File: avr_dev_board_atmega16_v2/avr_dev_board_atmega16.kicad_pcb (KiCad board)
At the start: 2 copper layers, 100 x 79 mm, 28 parts, among them J1 AVR-ISP-10, J2 DC 7-15V, J3 PA(0-7), J4 PC(0-7), J5 PB(0-4), J6 +5V, J7 PD(0-7), SW1 RESET, U1 ATmega16A-PU, U2 LM1117-5.0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

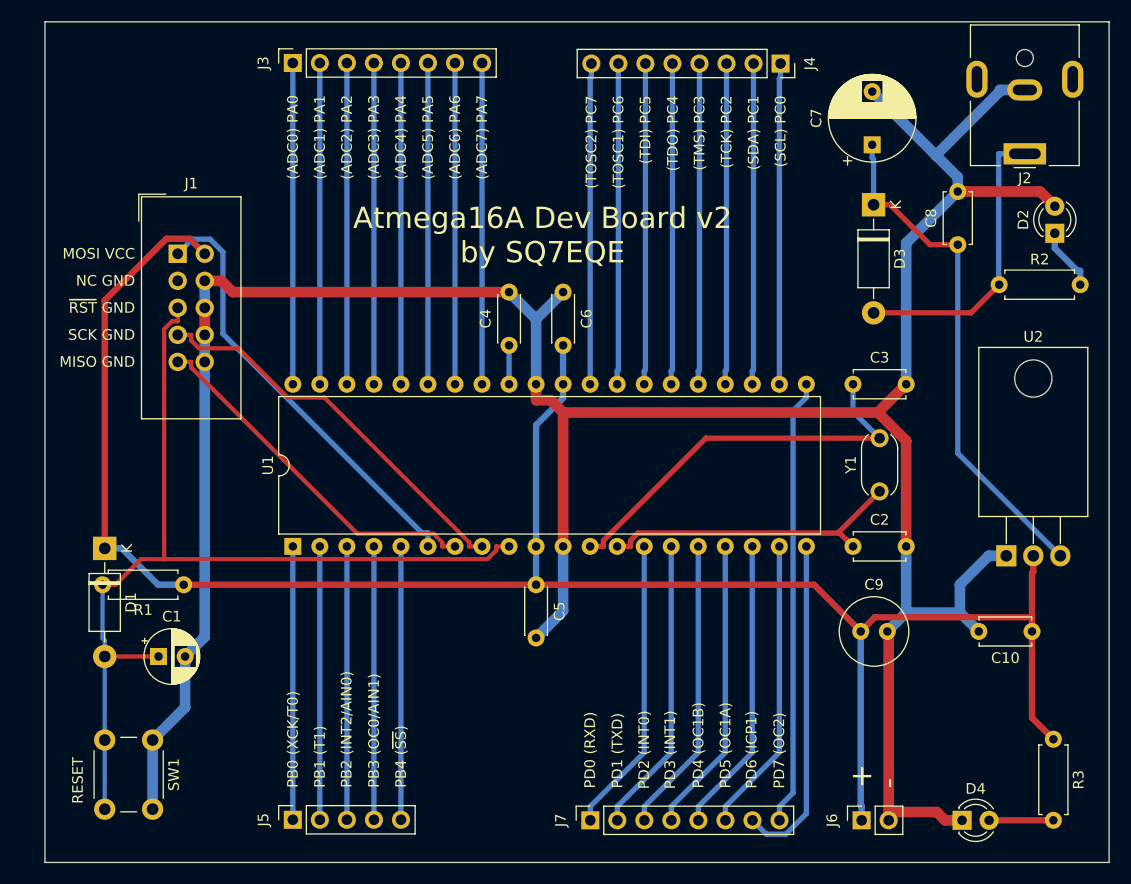
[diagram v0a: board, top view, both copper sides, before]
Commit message: update: I have fixed mistake in PCB layout, incorrect distribution of some components
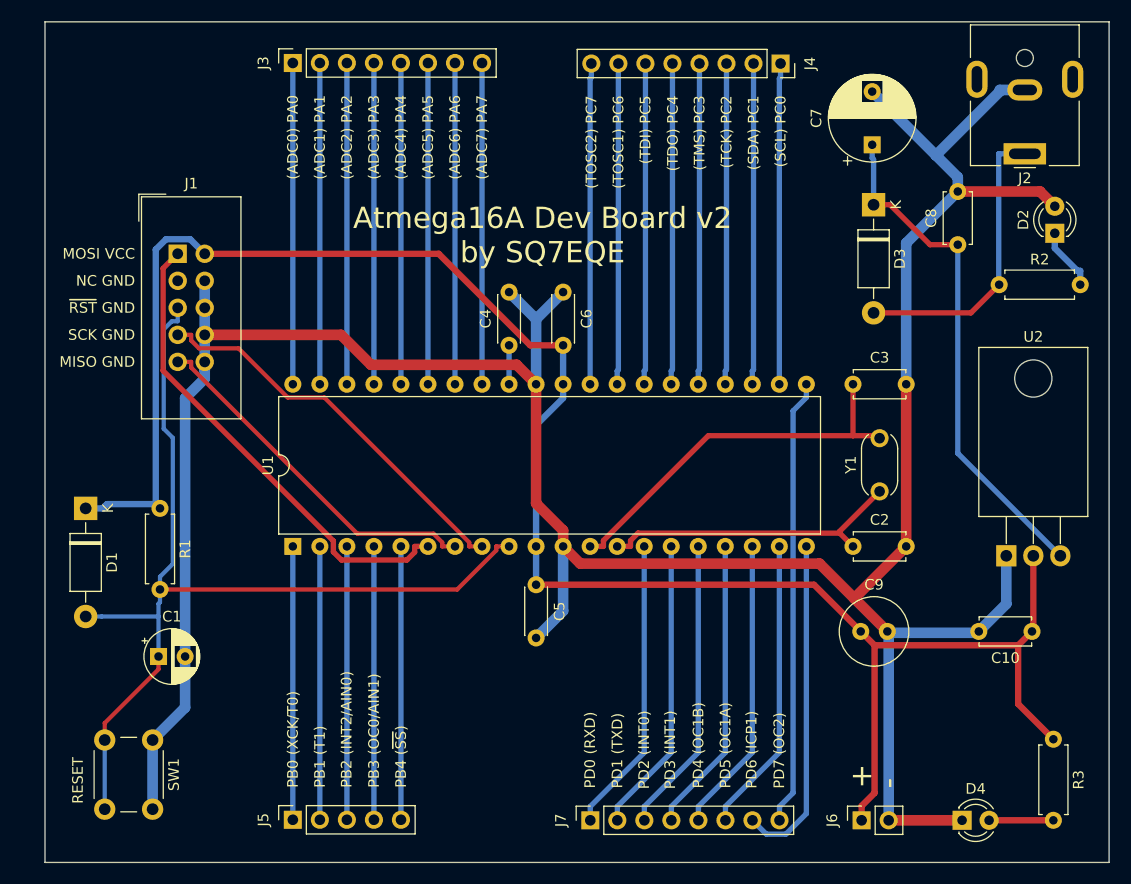
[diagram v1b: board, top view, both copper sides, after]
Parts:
- moved R1 7.51 mm to (51.0, 92.8), turned to 270 degrees
- moved D1 4.16 mm to (44.0, 92.8)
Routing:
- net +5V: track 186.1 -> 181.4 mm
- net GND: track 270.7 -> 274.8 mm
- net /MOSI: track 41.3 -> 45.3 mm
- net /RESET: track 90.6 -> 92.5 mm
- net Net-(C3-Pad1): track 37.8 -> 36.8 mm
